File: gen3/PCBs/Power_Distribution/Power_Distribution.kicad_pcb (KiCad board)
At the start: 2 copper layers, 130 x 80 mm, 71 parts, among them IC1 ACS713ELCTR-30A-T, IC2 ACS713ELCTR-30A-T, IC3 ACS713ELCTR-30A-T, IC4 ACS713ELCTR-30A-T, IC5 ACS713ELCTR-30A-T, IC6 ACS713ELCTR-30A-T, IC7 ACS713ELCTR-30A-T, IC8 ACS713ELCTR-30A-T, J1 Conn_01x02_Pin, J10 430450228, J11 430450228, J12 430450228, J13 430450228, J14 430450228, J15 430450228, J2 Conn_01x02_Pin, J3 SBH11-PBPC-D05-ST-BK, J4 1098169, J5 1098169, J6 1098169, J7 1098169, J8 430450228, J9 430450228, J98 Conn_01x08, J99 Conn_01x08, Q7 L78M05ABDT-TR, U1 MCP9808_MSOP, U3 AMS1117-3.3

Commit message: power dist final?
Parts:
- H2, H3, H4, H5: footprint MountingHole:MountingHole_3.2mm_M3 -> MountingHole:MountingHole_4.3mm_M4
- J10, J11, J12, J13, J14, J15, J9: footprint Imported_Footprints:CONN_SD-43045-010_02_MOL -> Connector_Molex:Molex_Micro-Fit_3.0_43045-0212_2x01_P3.00mm_Vertical
- J8: value 430450228 -> 0430450212; footprint Imported_Footprints:CONN_SD-43045-010_02_MOL -> Connector_Molex:Molex_Micro-Fit_3.0_43045-0212_2x01_P3.00mm_Vertical
- moved J10 2.07 mm to (166.8, 100.5), turned to 0 degrees
- moved J11 2.07 mm to (176.8, 100.5), turned to 0 degrees
- moved J12 2.07 mm to (186.8, 100.5), turned to 0 degrees
- moved J13 2.07 mm to (196.8, 100.5), turned to 0 degrees
- moved J14 2.07 mm to (206.7, 100.5), turned to 0 degrees
- moved J15 2.07 mm to (216.8, 100.4), turned to 0 degrees
- moved J8 2.07 mm to (146.8, 100.5), turned to 0 degrees
- moved J9 2.07 mm to (156.8, 100.5), turned to 0 degrees
- moved H3 1.09 mm to (230.1, 147.7)
- moved H5 0.94 mm to (87.9, 147.7)
- moved H4 0.67 mm to (87.9, 76.8)
- moved H2 0.36 mm to (230.1, 76.8)
- turned J3 to 180 degrees
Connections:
- J3 pad 1: PWM1 -> unconnected-(J3-Pad1)
- J3 pad 10: unconnected-(J3-Pad10) -> PWM1
- J3 pad 2: PWM2 -> GND
- J3 pad 3: PWM3 -> PWM8
- J3 pad 4: PWM4 -> PWM7
- J3 pad 5: PWM5 -> PWM6
- J3 pad 6: PWM6 -> PWM5
- J3 pad 7: PWM7 -> PWM4
- J3 pad 8: PWM8 -> PWM3
- J3 pad 9: GND -> PWM2
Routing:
- net PWM4: track 26.2 -> 24.0 mm
- net PWM5: track 25.1 -> 23.2 mm, vias 1 -> 0
- net PWM6: track 31.6 -> 29.6 mm
- net PWM3: track 26.7 -> 24.8 mm
- net PWM2: track 35.4 -> 33.4 mm
- net VIout2: track 66.4 -> 68.2 mm
- net VIout1: track 77.6 -> 79.3 mm
- net VIout8: track 81.1 -> 82.4 mm
- net PWM1: track 38.9 -> 37.8 mm
- net VIout3: track 54.8 -> 55.8 mm
- net VIout6: track 57.0 -> 58.0 mm
- net PWM7: track 33.3 -> 32.5 mm
- net PWM8: track 44.2 -> 43.6 mm
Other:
- board size 130 x 80 mm -> 151.4 x 80 mm

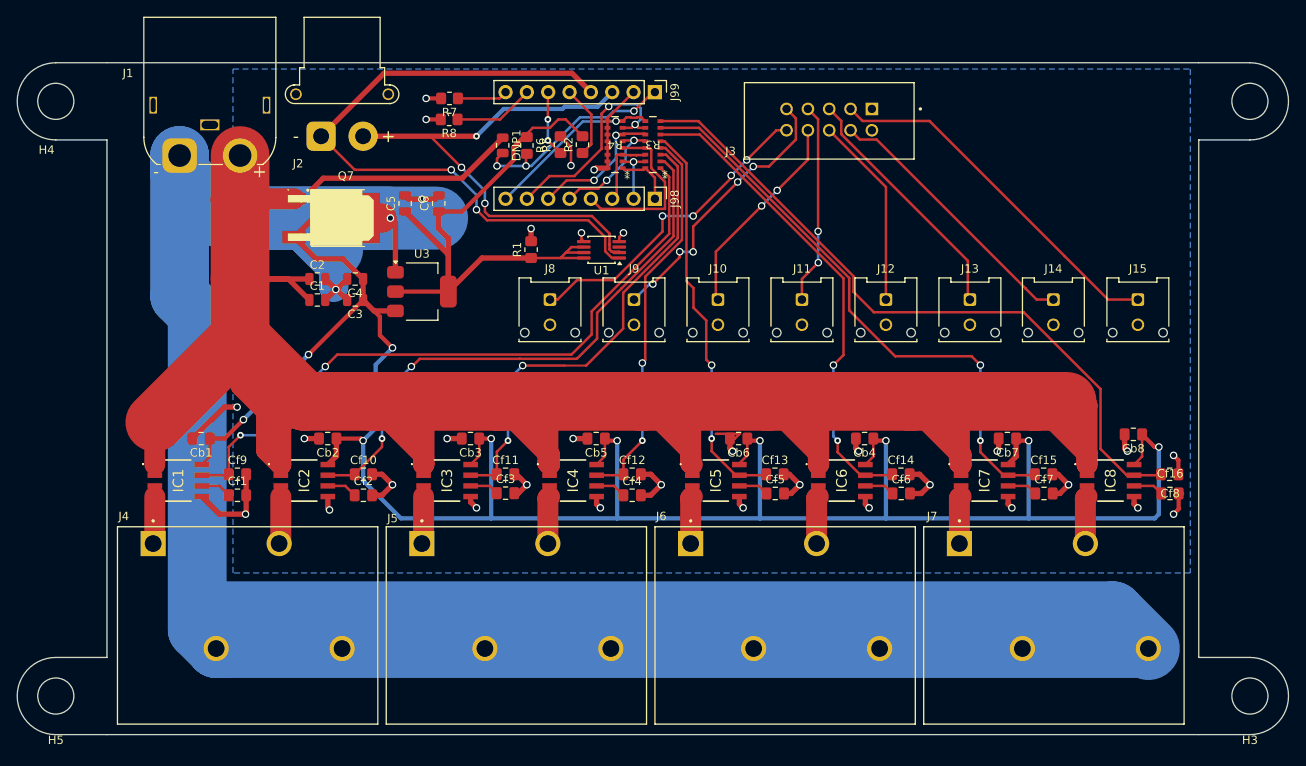
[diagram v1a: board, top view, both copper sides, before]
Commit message: power distribution board updates
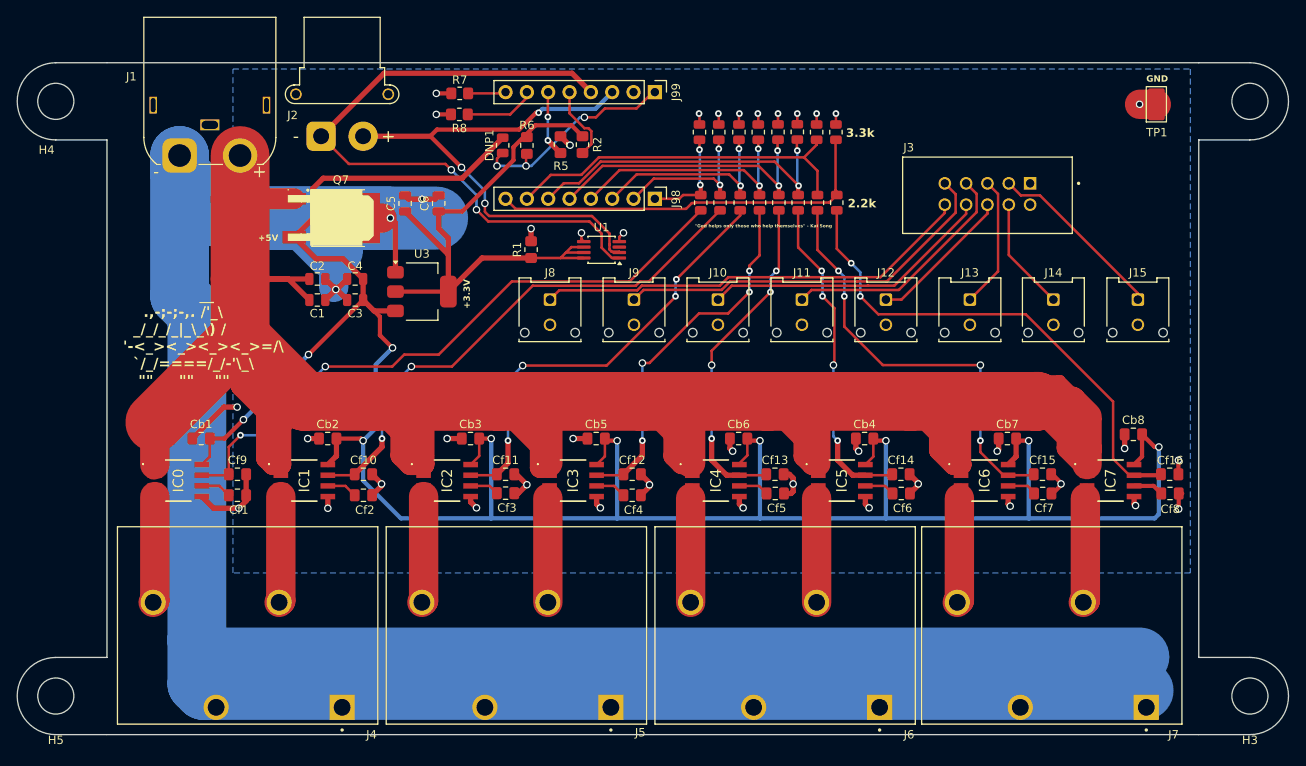
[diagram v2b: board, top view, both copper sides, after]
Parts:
- removed R3: 2.2k Array, Imported_Footprints:2506_8x_Resistor_Array
- removed R4: 3.3k Array, Imported_Footprints:2506_8x_Resistor_Array
- added R10: 2.2k, Resistor_SMD:R_0805_2012Metric, F.Cu at (167.0, 88.9)
- added R11: 2.2k, Resistor_SMD:R_0805_2012Metric, F.Cu at (169.4, 88.9)
- added R12: 2.2k, Resistor_SMD:R_0805_2012Metric, F.Cu at (171.7, 88.9)
- added R13: 2.2k, Resistor_SMD:R_0805_2012Metric, F.Cu at (174.0, 88.9)
- added R14: 2.2k, Resistor_SMD:R_0805_2012Metric, F.Cu at (176.3, 88.9)
- added R15: 2.2k, Resistor_SMD:R_0805_2012Metric, F.Cu at (178.6, 88.9)
- added R16: 2.2k, Resistor_SMD:R_0805_2012Metric, F.Cu at (180.9, 88.9)
- added R17: 3.3k, Resistor_SMD:R_0805_2012Metric, F.Cu at (164.6, 80.5)
- added R18: 3.3k, Resistor_SMD:R_0805_2012Metric, F.Cu at (166.8, 80.5)
- added R19: 3.3k, Resistor_SMD:R_0805_2012Metric, F.Cu at (169.2, 80.5)
- added R20: 3.3k, Resistor_SMD:R_0805_2012Metric, F.Cu at (171.6, 80.5)
- added R21: 3.3k, Resistor_SMD:R_0805_2012Metric, F.Cu at (173.9, 80.5)
- added R22: 3.3k, Resistor_SMD:R_0805_2012Metric, F.Cu at (176.2, 80.5)
- added R23: 3.3k, Resistor_SMD:R_0805_2012Metric, F.Cu at (178.5, 80.5)
- added R24: 3.3k, Resistor_SMD:R_0805_2012Metric, F.Cu at (180.8, 80.5)
- added R9: 2.2k, Resistor_SMD:R_0805_2012Metric, F.Cu at (164.7, 88.9)
- added TP1: TestPoint, TestPoint:TestPoint_Keystone_5019_Miniature, F.Cu at (218.9, 77.2)
- J10, J11, J12, J13, J14, J15, J9: value 430450228 -> 430450212
- J8: value 0430450212 -> 430450212
- moved J4 38.9 mm to (126.2, 127.5), turned to 180 degrees
- moved J5 38.9 mm to (158.2, 127.5), turned to 180 degrees
- moved J6 38.9 mm to (190.2, 127.5), turned to 180 degrees
- moved J7 38.7 mm to (222.0, 127.5), turned to 180 degrees
- moved J3 20.8 mm to (198.8, 87.9)
- moved R7 1.35 mm to (136.0, 75.9)
- moved R8 1.35 mm to (136.0, 78.4)
- moved Cf15 0.15 mm to (205.4, 121.2)
- moved Cf7 0.15 mm to (205.4, 123.5)
- renumbered IC1 to IC0, IC2 to IC1, IC3 to IC2, IC4 to IC3, IC5 to IC4, IC6 to IC5, IC7 to IC6, IC8 to IC7
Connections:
- Cf10 pad 1: VIout2 -> VIout1
- Cf11 pad 1: VIout3 -> VIout2
- Cf12 pad 1: VIout4 -> VIout3
- Cf13 pad 1: VIout5 -> VIout4
- Cf14 pad 1: VIout6 -> VIout5
- Cf15 pad 1: VIout7 -> VIout6
- Cf16 pad 1: VIout8 -> VIout7
- Cf9 pad 1: VIout1 -> VIout0
- IC0 pad 3: PWR1 -> PWR0
- IC0 pad 4: PWR1 -> PWR0
- IC0 pad 7: VIout1 -> VIout0
- IC1 pad 3: PWR2 -> PWR1
- IC1 pad 4: PWR2 -> PWR1
- IC1 pad 7: VIout2 -> VIout1
- IC2 pad 3: PWR3 -> PWR2
- IC2 pad 4: PWR3 -> PWR2
- IC2 pad 7: VIout3 -> VIout2
- IC3 pad 3: PWR4 -> PWR3
- IC3 pad 4: PWR4 -> PWR3
- IC3 pad 7: VIout4 -> VIout3
- IC4 pad 3: PWR5 -> PWR4
- IC4 pad 4: PWR5 -> PWR4
- IC4 pad 7: VIout5 -> VIout4
- IC5 pad 3: PWR6 -> PWR5
- IC5 pad 4: PWR6 -> PWR5
- IC5 pad 7: VIout6 -> VIout5
- IC6 pad 3: PWR7 -> PWR6
- IC6 pad 4: PWR7 -> PWR6
- IC6 pad 7: VIout7 -> VIout6
- IC7 pad 3: PWR8 -> PWR7
- IC7 pad 4: PWR8 -> PWR7
- IC7 pad 7: VIout8 -> VIout7
- J10 pad 1: PWM3 -> PWM2
- J11 pad 1: PWM4 -> PWM3
- J12 pad 1: PWM5 -> PWM4
- J13 pad 1: PWM6 -> PWM5
- J14 pad 1: PWM7 -> PWM6
- J15 pad 1: PWM8 -> PWM7
- J3 pad 10: PWM1 -> PWM0
- J3 pad 3: PWM8 -> PWM7
- J3 pad 4: PWM7 -> PWM6
- J3 pad 5: PWM6 -> PWM5
- J3 pad 6: PWM5 -> PWM4
- J3 pad 7: PWM4 -> PWM3
- J3 pad 8: PWM3 -> PWM2
- J3 pad 9: PWM2 -> PWM1
- J4 pad 1: PWR1 -> -BATT
- J4 pad 2: -BATT -> PWR1
- J4 pad 3: PWR2 -> -BATT
- J4 pad 4: -BATT -> PWR0
- J5 pad 1: PWR3 -> -BATT
- J5 pad 2: -BATT -> PWR3
- J5 pad 3: PWR4 -> -BATT
- J5 pad 4: -BATT -> PWR2
- J6 pad 1: PWR5 -> -BATT
- J6 pad 2: -BATT -> PWR5
- J6 pad 3: PWR6 -> -BATT
- J6 pad 4: -BATT -> PWR4
- J7 pad 1: PWR7 -> -BATT
- J7 pad 2: -BATT -> PWR7
- J7 pad 3: PWR8 -> -BATT
- J7 pad 4: -BATT -> PWR6
- J8 pad 1: PWM1 -> PWM0
- J9 pad 1: PWM2 -> PWM1
- J98 pad 1: VIout1Div -> VIout0Div
- J98 pad 2: VIout2Div -> VIout1Div
- J98 pad 3: VIout3Div -> VIout2Div
- J98 pad 4: VIout4Div -> VIout3Div
- J98 pad 5: VIout5Div -> VIout4Div
- J98 pad 6: VIout6Div -> VIout5Div
- J98 pad 7: VIout7Div -> VIout6Div
- J98 pad 8: VIout8Div -> VIout7Div
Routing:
- net VIout8: track 82.4 -> 0.00 mm
- net VIout0: track 0.00 -> 74.4 mm, vias 0 -> 2
- net PWM0: track 0.00 -> 52.3 mm
- net PWM8: track 43.6 -> 0.00 mm
- net +BATT: track 301.4 -> 329.2 mm
- net VIout6Div: track 16.4 -> 43.1 mm, vias 2 -> 0
- net VIout5Div: track 14.2 -> 39.6 mm
- net VIout7Div: track 26.1 -> 47.3 mm, vias 2 -> 0
- net GND: track 105.6 -> 84.6 mm, vias 31 -> 39
- net VIout8Div: track 20.9 -> 0.00 mm, vias 1 -> 0
- net VIout3Div: track 8.86 -> 28.9 mm, vias 0 -> 2
- net VIout2Div: track 7.21 -> 23.7 mm, vias 1 -> 2
- net PWM6: track 29.6 -> 13.5 mm
- net VIout1: track 79.3 -> 63.3 mm
- net VIout2: track 68.2 -> 52.5 mm, vias 2 -> 4
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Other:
- board text added: "+3.3V"
- board text added: "+5V"
- board text added: "2.2k"
- board text added: "3.3k"
- board text added: "GND"
- board text added: "R18"
- board text added: "__ .,-;-;-,. /'_\ _/_/_/_|_\_\) / '-<_><_><_><_>=/\ `/_/====/_/-'\_\ {dblquote}{dblquote} {dblquote}{dblquote} {dblquote}{dblquote}"
- board text added: "{dblquote}God helps only those who help themselves{dblquote} - Kai Song"
